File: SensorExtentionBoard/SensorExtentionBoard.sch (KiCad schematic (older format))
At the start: 24 parts, among them J1 Conn_01x02_Male, J2 Conn_01x02_Male, J3 Conn_02x03_Top_Bottom, J4 Conn_01x02_Male, U1 TCA9544A, U2 TCA9555DBR

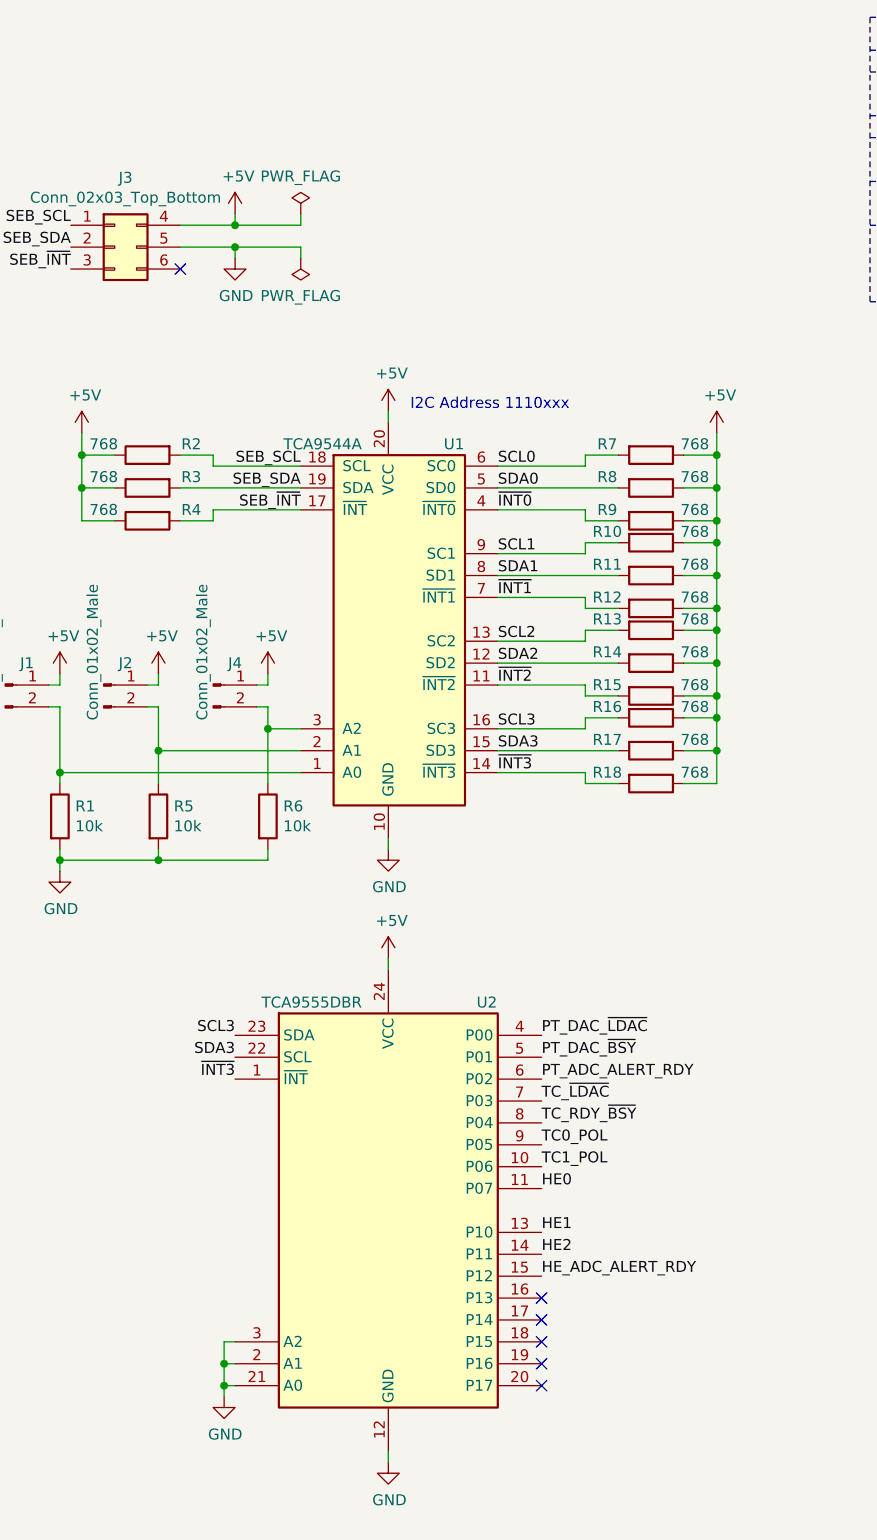
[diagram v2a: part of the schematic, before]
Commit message: Added decoupling caps
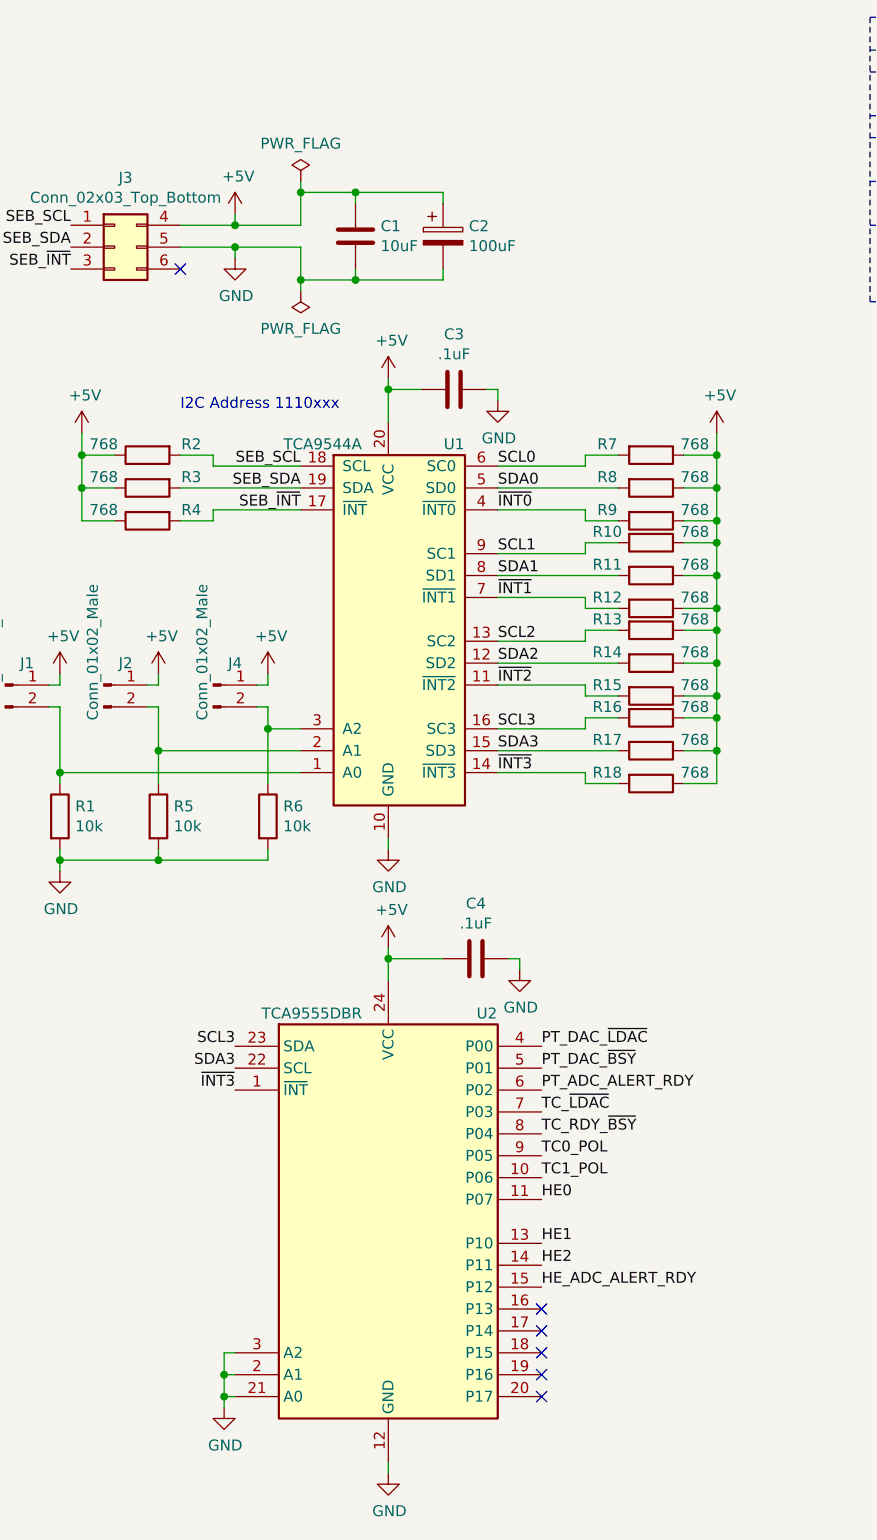
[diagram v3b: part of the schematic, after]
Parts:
- added C1: 10uF, symbol Device:C
- added C2: 100uF, symbol Device:CP
- added C3, C4: .1uF, symbol Device:C
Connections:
- net +5V: now also C1.1, C2.1, C3.2, C4.2
- net GND: now also C1.2, C2.2, C3.1, C4.1
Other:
- moved on the sheet: U2

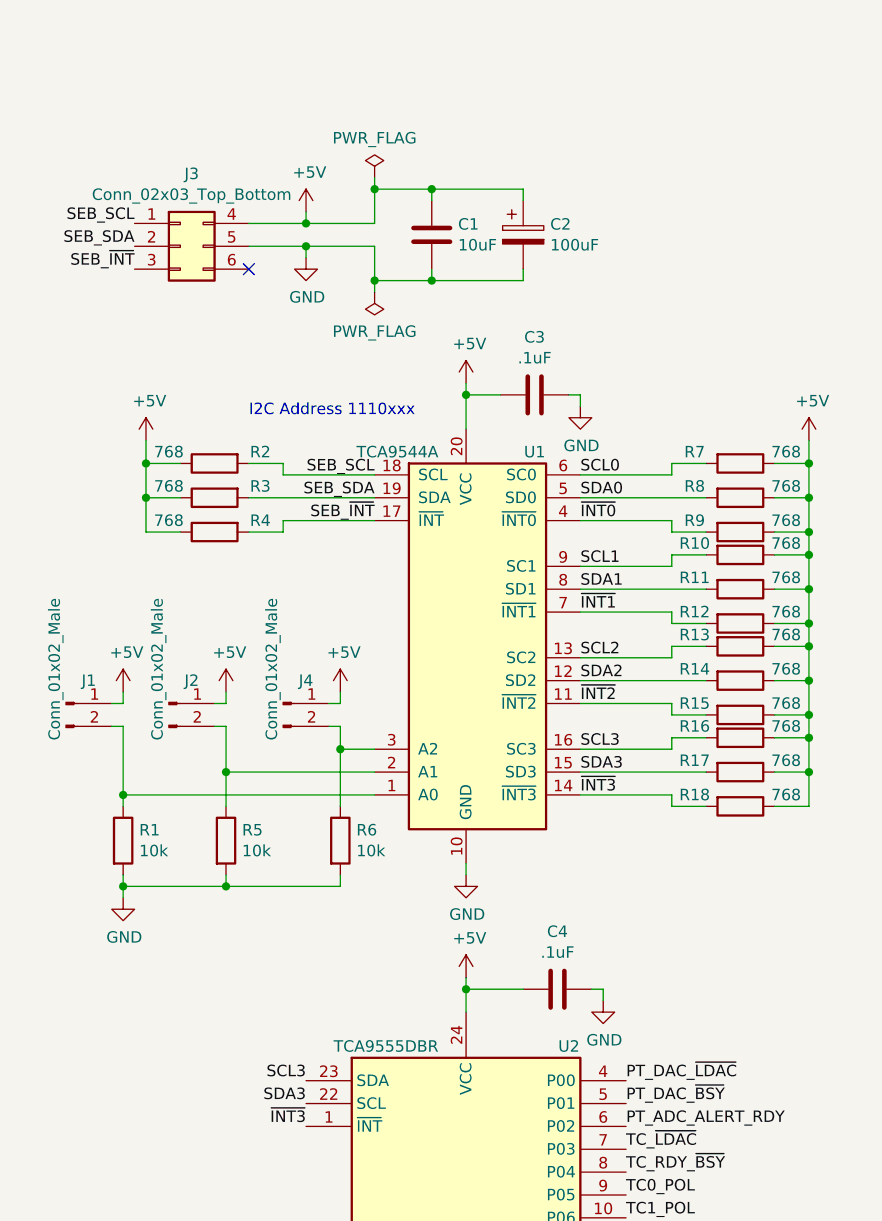
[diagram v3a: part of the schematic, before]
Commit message: Replaced ADS1115 with ADS1015 on PT page
The ADS1115 is being used to read the voltages provided by the Helix
system to the pressure transducers. The ADS1015 is already doing
the same job for the Hall Effect sensors, however the ADS1015 has
4 bits lower accuracy. High accuracy is not needed for this
application so be replacing the ADS1115 with the ADS1015 we can
reduce cost and more importantly reduce BOM size making the project
logistics easier to manage.
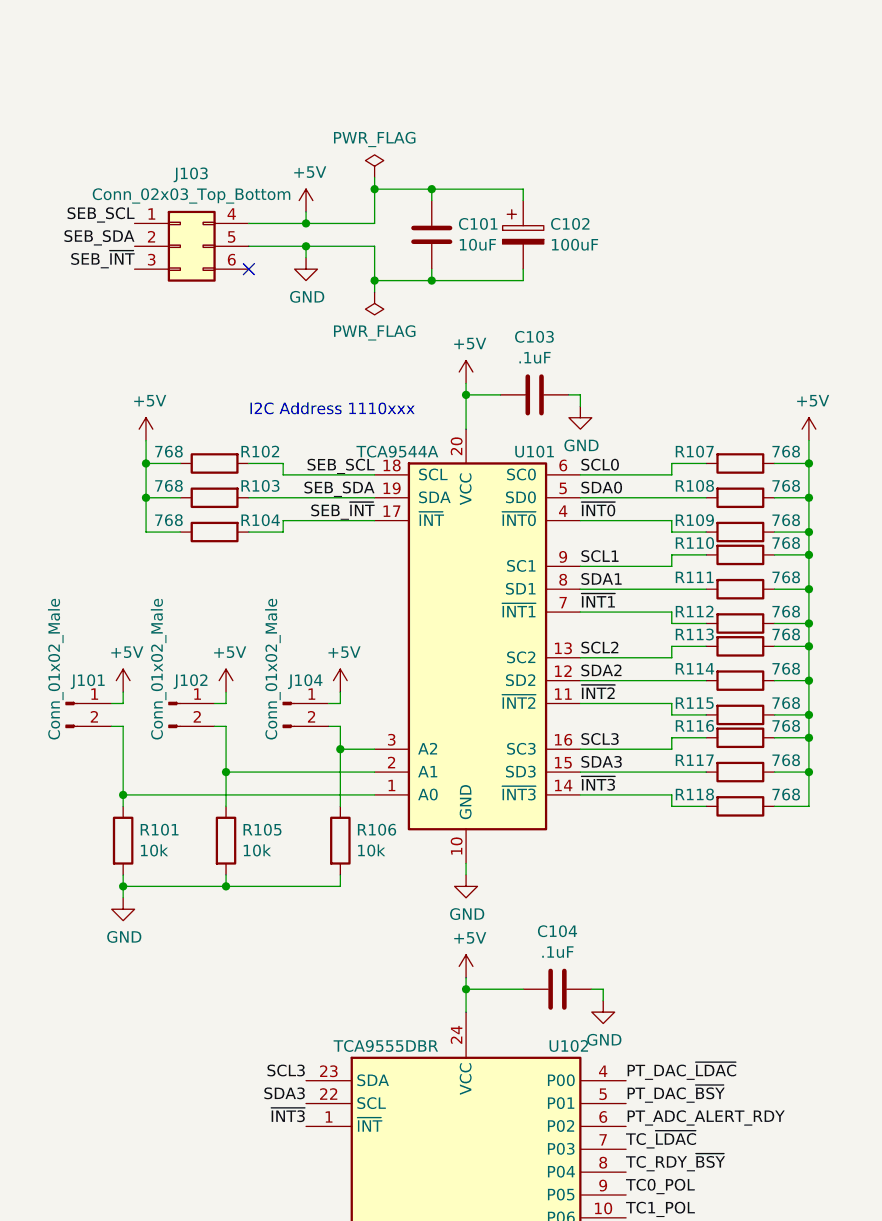
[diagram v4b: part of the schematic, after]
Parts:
- renumbered C1 to C101, C2 to C102, C3 to C103, C4 to C104, J1 to J101, J2 to J102, J3 to J103, J4 to J104, R1 to R101, R2 to R102, R3 to R103, R4 to R104, R5 to R105, R6 to R106, R7 to R107, R8 to R108, R9 to R109, R10 to R110, R11 to R111, R12 to R112, R13 to R113, R14 to R114, R15 to R115, R16 to R116, R17 to R117, R18 to R118, U1 to U101, U2 to U102

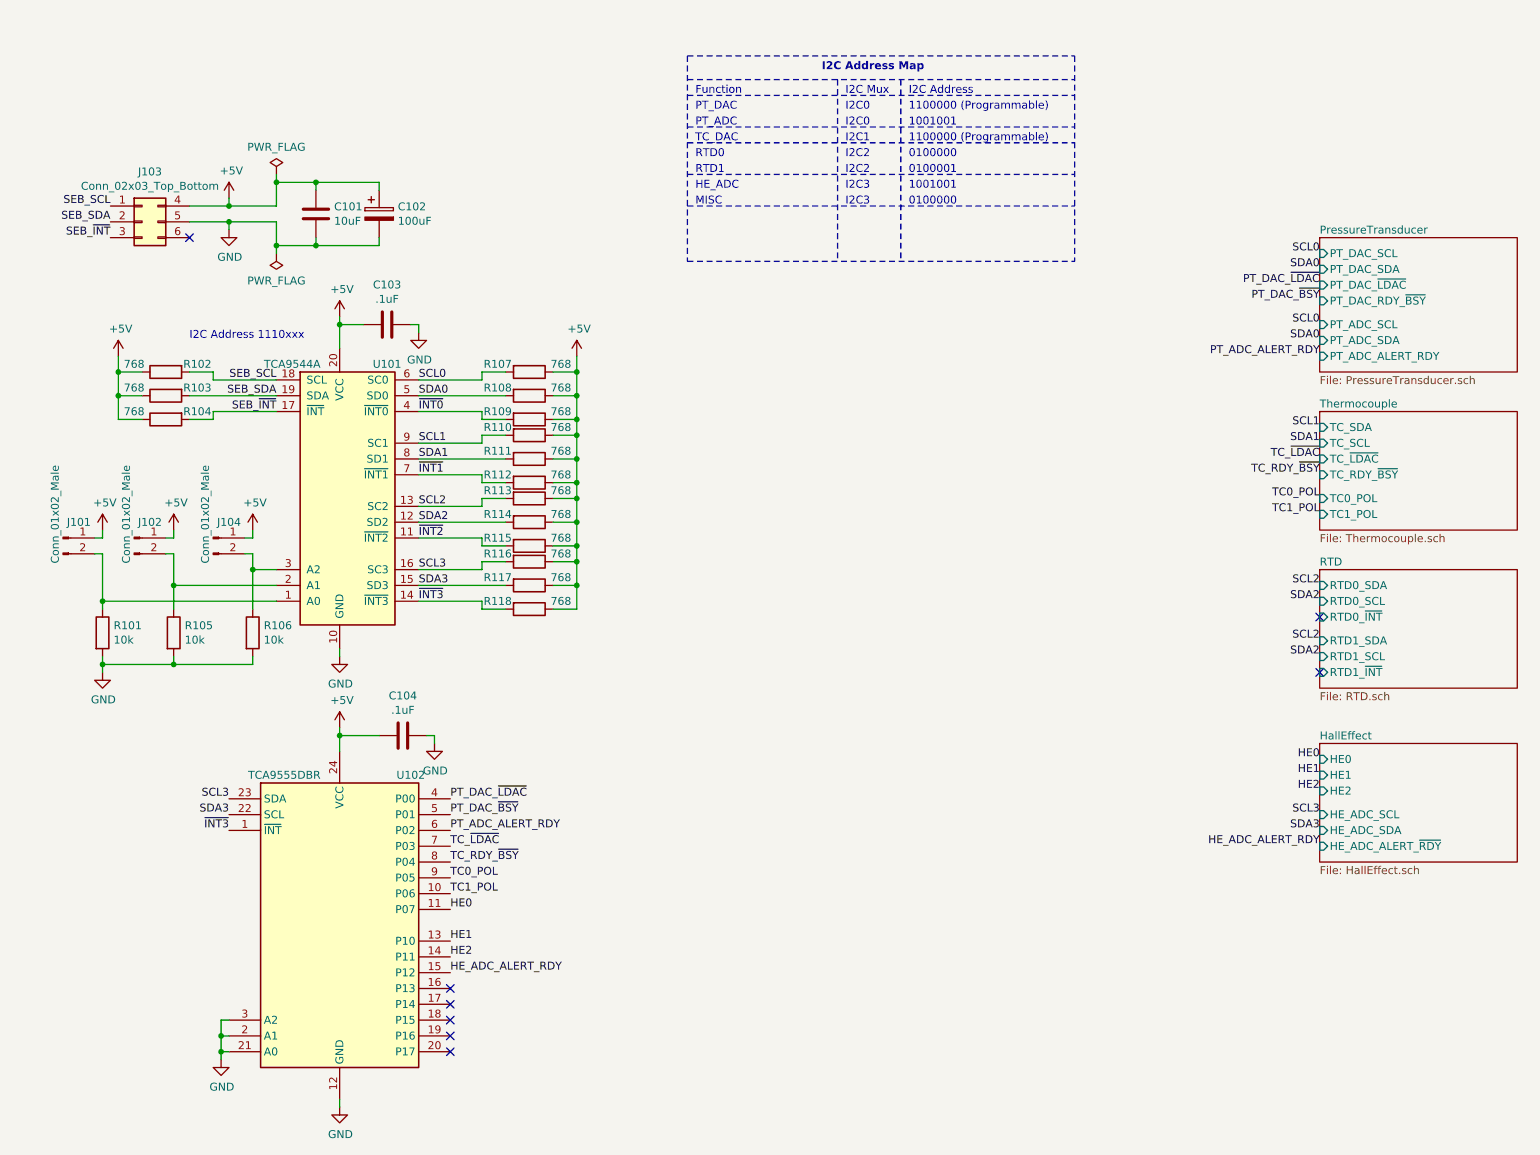
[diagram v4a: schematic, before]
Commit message: Added header for programming the EEPROM memory on the SEB
Adding this header may allow the test rig to load new memory configs
onto the SEB under test prior to running tests. This will allow
greater ability for automation of testing when the new software
requires a change to the config onboard the SEB.
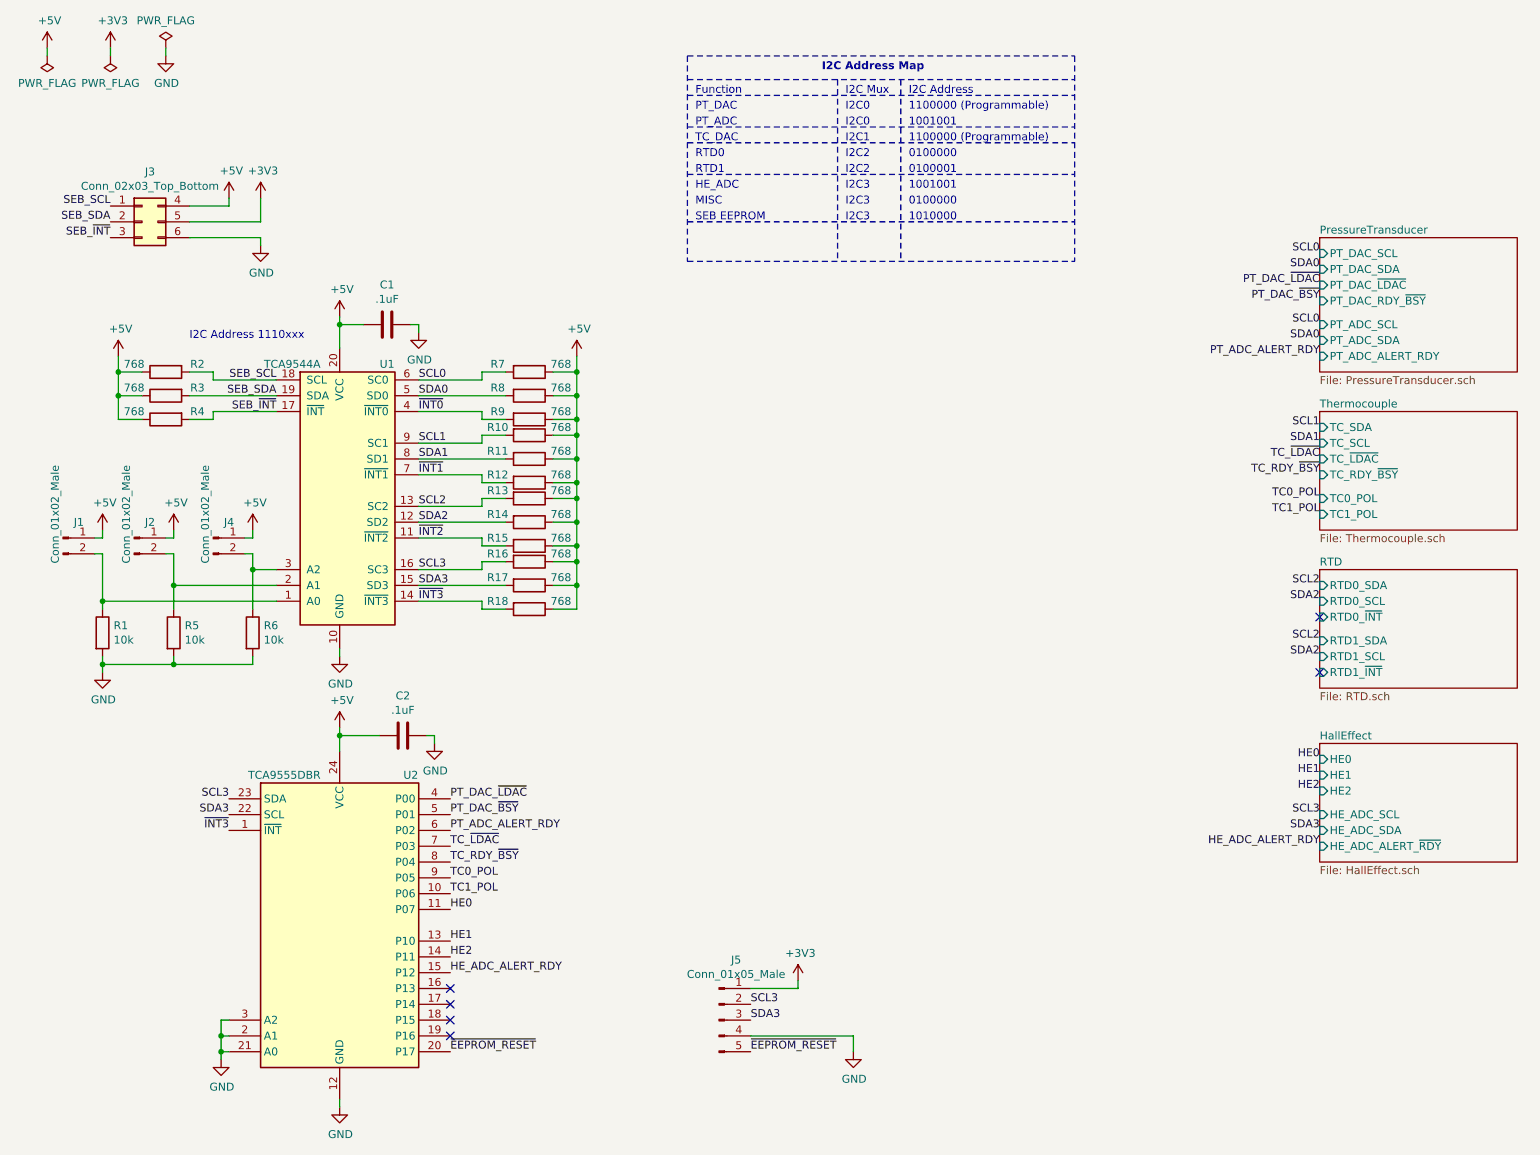
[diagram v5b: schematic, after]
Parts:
- removed C101: 10uF, symbol Device:C
- removed C102: 100uF, symbol Device:CP
- added J5: Conn_01x05_Male, Connector_Molex:Molex_MicroClasp_55932-0510_1x05_P2.00mm_Vertical, symbol Connector:Conn_01x05_Male
- renumbered C103 to C1, C104 to C2, J101 to J1, J102 to J2, J103 to J3, J104 to J4, R101 to R1, R110 to R10, R111 to R11, R112 to R12, R113 to R13, R114 to R14, R115 to R15, R116 to R16, R117 to R17, R118 to R18, R102 to R2, R103 to R3, R104 to R4, R105 to R5, R106 to R6, R107 to R7, R108 to R8, R109 to R9, U101 to U1, U102 to U2
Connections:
- net GND: now also J3.6 (Pin_6), J5.4 (Pin_4); no longer J3.5 (Pin_5)
- net SCL3: now also J5.2 (Pin_2)
- net SDA3: now also J5.3 (Pin_3)
- net ~EEPROM_RESET: now reaches U2.20 (P17)
- net ~EEPROM_RESET: now also J5.5 (Pin_5)
- new net +3V3: J3.5 (Pin_5), J5.1 (Pin_1)
- no-connect marks 8 -> 6
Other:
- note added: "1010000"
- note added: "SEB EEPROM"
